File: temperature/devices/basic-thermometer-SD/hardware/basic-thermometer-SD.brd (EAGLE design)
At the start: 22.9 x 30.5 mm, 21 parts, among them IC1 MEGA8-AI

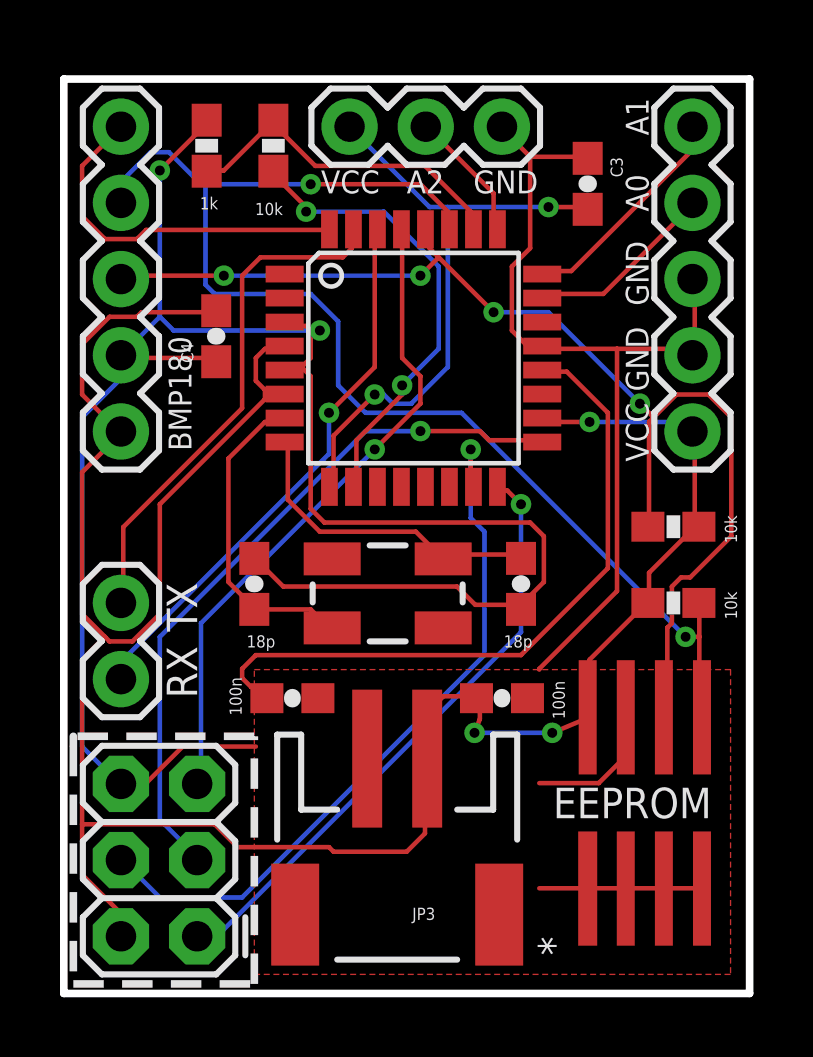
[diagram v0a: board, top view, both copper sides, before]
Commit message: moving components into subfolders
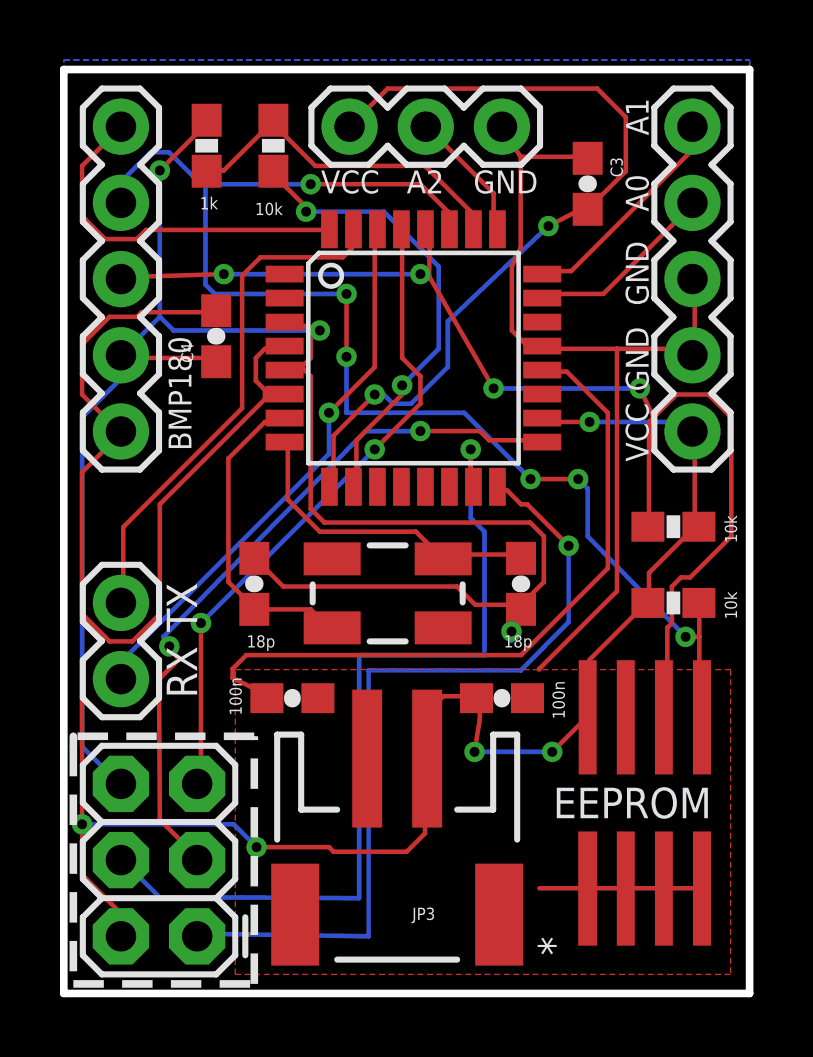
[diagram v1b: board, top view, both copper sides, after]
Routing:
- net GND: track 107.4 -> 98.9 mm, vias 2 -> 3
- net MISO: track 20.3 -> 27.7 mm
- net PD5: track 21.2 -> 28.2 mm
- net MOSI: track 24.3 -> 29.1 mm
- net SDA: track 43.2 -> 45.3 mm, vias 2 -> 6
- net VCC: track 80.8 -> 81.8 mm, vias 3 -> 5
- net SCL: track 39.5 -> 40.3 mm
- net AREF: track 23.0 -> 23.5 mm
- net SCK: track 23.7 -> 24.0 mm, vias 1 -> 2
- net RST: vias 1 -> 2
- added copper zone on layer 16, net GND
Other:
- board size 22.9 x 30.5 mm -> 22.9 x 30.8 mm
